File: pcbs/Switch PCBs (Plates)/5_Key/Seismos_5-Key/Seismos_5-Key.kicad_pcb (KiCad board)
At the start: 2 copper layers, 19 x 105.4 mm, 14 parts, among them J1 SM10B-SRSS-TB_(LF)(SN), SW1 Switch_SK6812-E_Diode, SW2 Switch_SK6812-E_Diode, SW3 Switch_SK6812-E_Diode, SW4 Switch_SK6812-E_Diode, SW5 Switch_SK6812-E_Diode

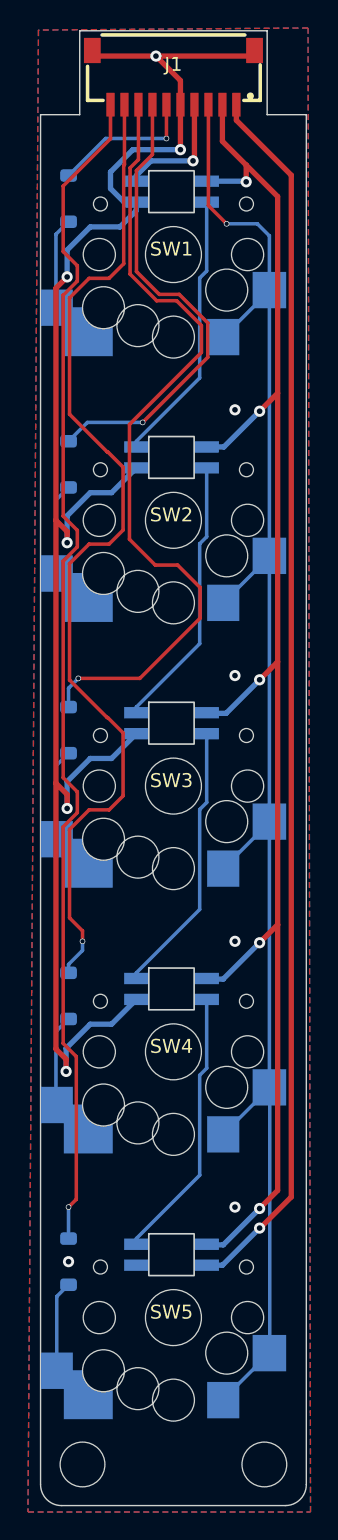
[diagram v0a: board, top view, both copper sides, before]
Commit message: Added stencils for new and old PCBs
Created stencils for solder pasting PCBs with the core and plates.
I ordered both new and old versions so two stencils were made; however,
the holes for the old variant are misaligned. For this, use the other
aligning holes.

In addition, repaired footprints for switches where the switch footprint
was appearing on the reverse side. This is now fixed.
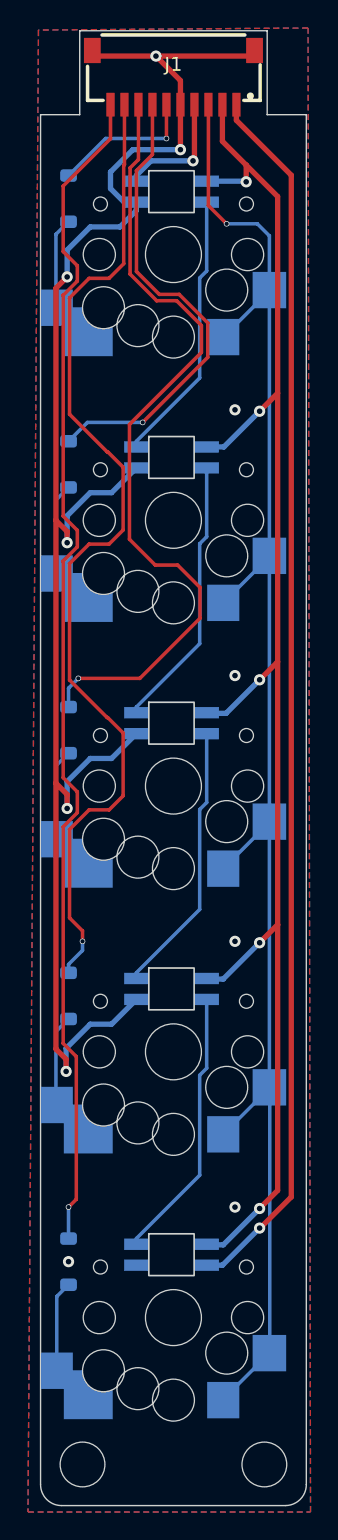
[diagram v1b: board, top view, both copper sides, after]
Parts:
- SW1, SW2, SW3, SW4, SW5: moved to B.Cu
- turned SW1 to 180 degrees
- turned SW2 to 180 degrees
- turned SW3 to 180 degrees
- turned SW4 to 180 degrees
- turned SW5 to 180 degrees

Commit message: Release v1.1
***NOTE***: If you have a previous commit, please update your files.
This commit fixes the incorrect RGB pinout and power switch as the
RGB footprint was incorrect.
The power switch behaviour is also fixed in this commit so the position
matches on both sides.
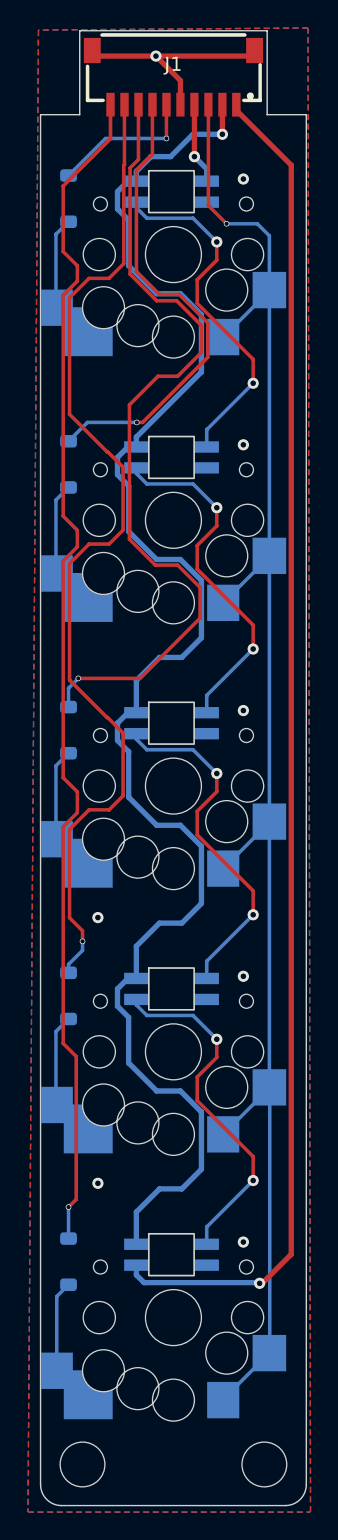
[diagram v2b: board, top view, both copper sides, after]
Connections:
- SW5 pad GND: unconnected-(SW5-PadGND) -> GND
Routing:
- net GND: track 122.3 -> 15.8 mm, vias 11 -> 8
- net /RGB_Out: track 87.3 -> 96.3 mm
- net Net-(SW3B-DOUT): track 19.6 -> 25.4 mm, vias 0 -> 2
- net Net-(SW4B-DOUT): track 19.6 -> 25.4 mm, vias 0 -> 2
- net Net-(SW1B-DOUT): track 19.6 -> 25.4 mm, vias 0 -> 2
- net Net-(SW2B-DOUT): track 19.6 -> 25.4 mm, vias 0 -> 2
- net /V+: track 109.5 -> 114.2 mm, vias 5 -> 1
- net /RGB_In: track 8.55 -> 5.83 mm
- net /Row3: track 57.5 -> 58.3 mm
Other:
- board text added: "Rev. 1.1"
- board text removed: "Rev. 1.0"
